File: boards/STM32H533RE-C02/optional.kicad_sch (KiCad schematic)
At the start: 17 parts, among them J1 Conn_01x20_Pin, J2 Conn_01x20_Pin, J3 Qwiic_connector, J4 SD Card slot, J5 SD Card slot, U4 74LS125

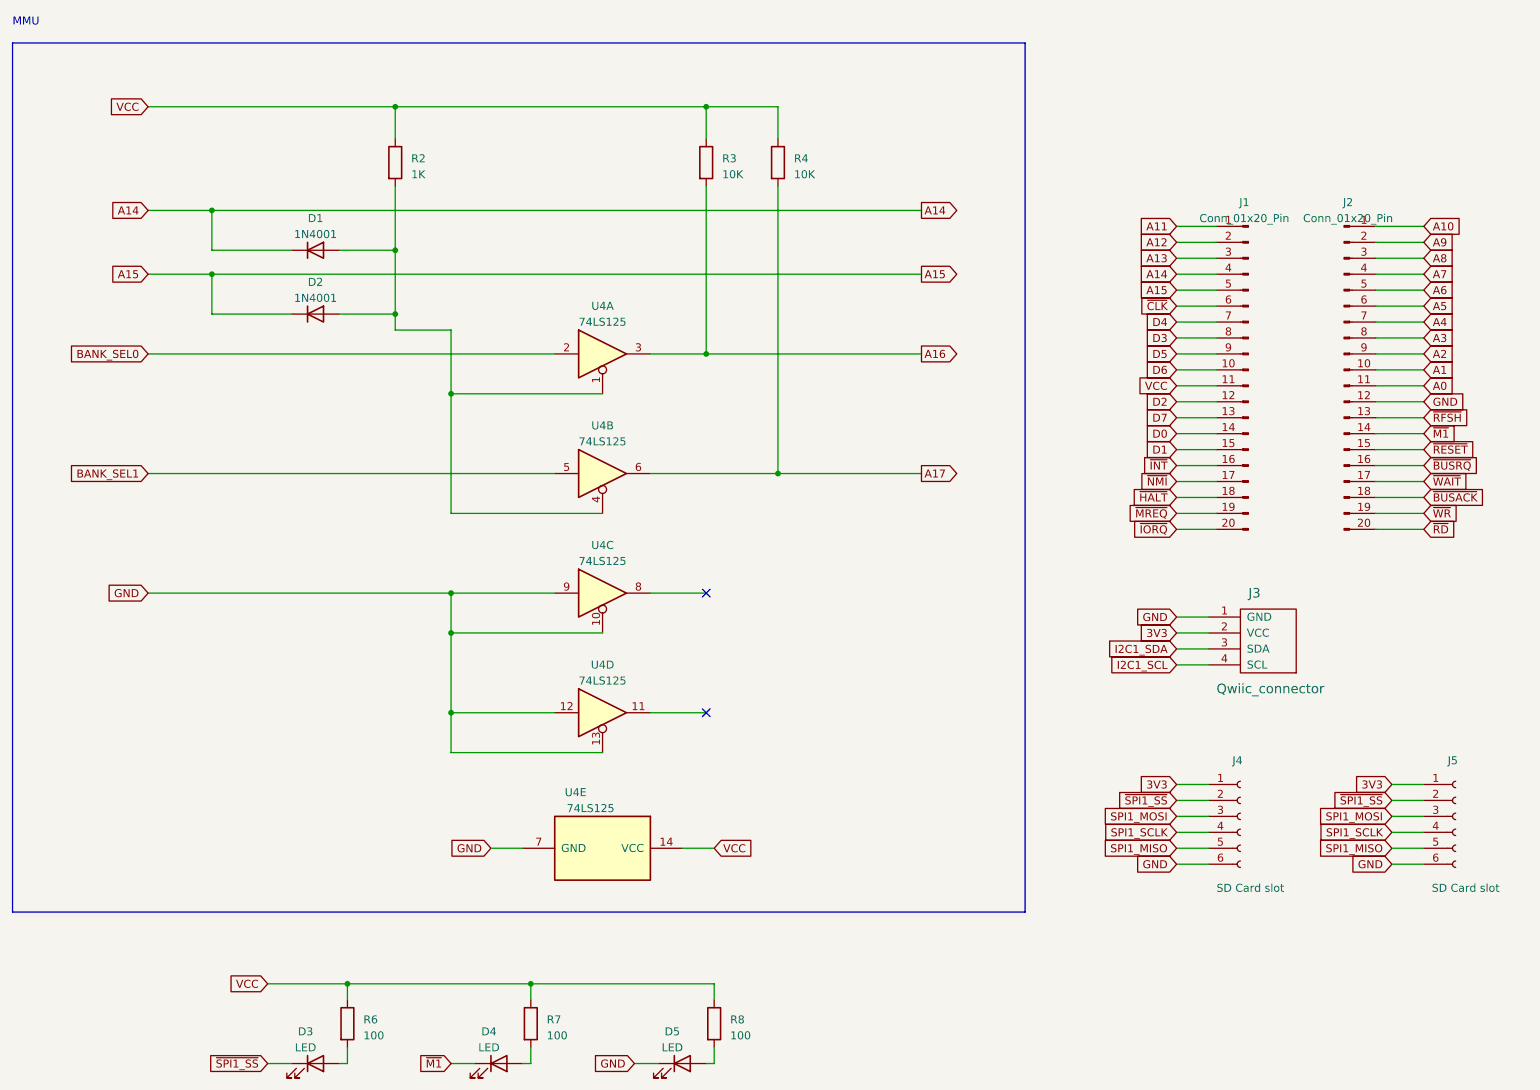
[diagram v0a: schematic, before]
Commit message: stm32h533re: Fix schematics
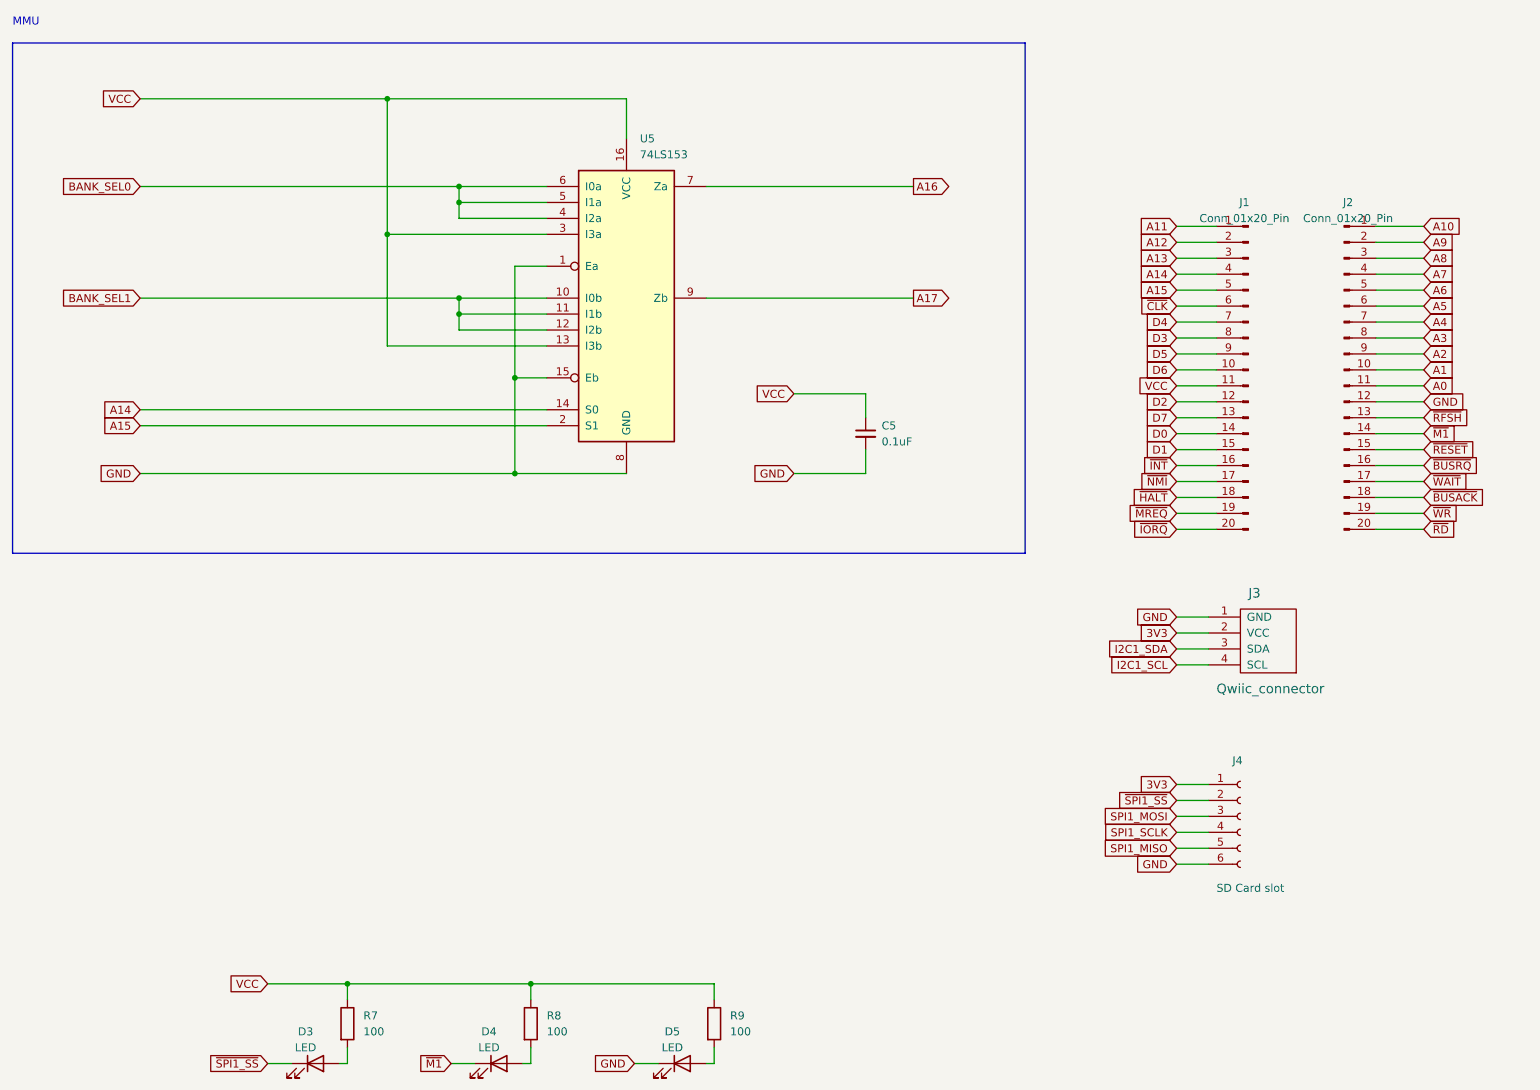
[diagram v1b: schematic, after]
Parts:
- removed D1, D2: 1N4001, Diode_SMD:D_0805_2012Metric_Pad1.15x1.40mm_HandSolder, symbol Diode:1N4001
- removed J5: SD Card slot, Connector_PinHeader_2.54mm:PinHeader_1x06_P2.54mm_Vertical, symbol Connector:Conn_01x06_Socket
- removed R2: 1K, Resistor_SMD:R_0805_2012Metric_Pad1.20x1.40mm_HandSolder, symbol Device:R
- removed R3, R4: 10K, Resistor_SMD:R_0805_2012Metric_Pad1.20x1.40mm_HandSolder, symbol Device:R
- removed U4: 74LS125, Package_SO:SSOP-14_5.3x6.2mm_P0.65mm, symbol 74xx:74LS125
- added C5: 0.1uF, Capacitor_THT:C_Disc_D3.8mm_W2.6mm_P2.50mm, symbol Device:C_Small
- added U5: 74LS153, Package_SO:SOP-16_4.55x10.3mm_P1.27mm, symbol 74xx:74LS153
- J3: symbol mylib:Qwiic_connector -> library:Qwiic_connector
- renumbered R6 to R7, R7 to R8, R8 to R9
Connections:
- net A14: now also U5.14 (S0)
- net A15: now also U5.2 (S1)
- net A16: now also U5.7 (Za)
- net A17: now also U5.9 (Zb)
- net BANK_SEL0: now also U5.4 (I2a), U5.5 (I1a), U5.6 (I0a)
- net BANK_SEL1: now also U5.10 (I0b), U5.11 (I1b), U5.12 (I2b)
- net GND: now also C5.2, U5.1 (Ea), U5.15 (Eb), U5.8 (GND)
- net VCC: now also C5.1, U5.13 (I3b), U5.16 (VCC), U5.3 (I3a)
- no-connect marks 2 -> 0
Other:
- title: Nucleo64 Z80 -> Nucleo64 Z80 (H533)

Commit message: stm32h533re: Fix PCB layout
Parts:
- C5: footprint Capacitor_THT:C_Disc_D3.8mm_W2.6mm_P2.50mm -> Capacitor_SMD:C_0603_1608Metric_Pad1.08x0.95mm_HandSolder
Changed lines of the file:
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@@
 			)
 		)
-		(property "Footprint" "Capacitor_THT:C_Disc_D3.8mm_W2.6mm_P2.50mm"
+		(property "Footprint" "Capacitor_SMD:C_0603_1608Metric_Pad1.08x0.95mm_HandSolder"
 			(at 161.29 82.55 0)
 			(effects
